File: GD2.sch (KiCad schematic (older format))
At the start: 19 parts, among them IC15 HCPL-316J, IC16 IXDD614PI, P16 CONN_01X03, P17 CONN_01X03

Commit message: uding HCPL-361J modified symbol
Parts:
- IC15: symbol HCPL-316J-RESCUE-gatedrive -> HCPL-316J
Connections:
- wire segments 41 -> 50
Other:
- moved on the sheet: IC16
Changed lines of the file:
@@
 EESchema Schematic File Version 2
-LIBS:gatedrive-rescue
 LIBS:power
 LIBS:device
@@
 LIBS:contrib
 LIBS:valves
-LIBS:GateDrive
+LIBS:74xgxx
+LIBS:ac-dc
+LIBS:actel
+LIBS:Altera
+LIBS:analog_devices
+LIBS:brooktre
+LIBS:cmos_ieee
+LIBS:dc-dc
+LIBS:diode
+LIBS:elec-unifil
+LIBS:ESD_Protection
+LIBS:ftdi
+LIBS:gennum
+LIBS:graphic
+LIBS:hc11
+LIBS:ir
+LIBS:Lattice
+LIBS:logo
+LIBS:maxim
+LIBS:microchip_dspic33dsc
+LIBS:microchip_pic10mcu
+LIBS:microchip_pic12mcu
+LIBS:microchip_pic16mcu
+LIBS:microchip_pic18mcu
+LIBS:microchip_pic32mcu
+LIBS:motor_drivers
+LIBS:msp430
+LIBS:nordicsemi
+LIBS:nxp_armmcu
+LIBS:onsemi
+LIBS:Oscillators
+LIBS:powerint
+LIBS:Power_Management
+LIBS:pspice
+LIBS:references
+LIBS:relays
+LIBS:rfcom
+LIBS:sensors
+LIBS:silabs
+LIBS:stm8
+LIBS:stm32
+LIBS:supertex
+LIBS:switches
+LIBS:transf
+LIBS:ttl_ieee
+LIBS:video
+LIBS:Worldsemi
+LIBS:Xicor
+LIBS:Zilog
 LIBS:gatedrive-cache
 EELAYER 25 0
@@
 L IXDD614PI-RESCUE-gatedrive IC16
 U 1 1 56EF8E42
-P 7900 5100
-F 0 "IC16" H 7900 4900 60  0000 C CNN
-F 1 "IXDD614PI" H 7950 5450 60  0000 C CNN
-F 2 "gatedrive:DIP-8_W7.62mm_LongPads" H 7900 5200 60  0001 C CNN
-F 3 "" H 7900 5200 60  0000 C CNN
-F 4 "CHINA[already bought]" H 7900 5100 60  0001 C CNN "Supplier"
-	1    7900 5100
-	1    0    0    -1
-$EndComp
-$Comp
-L HCPL-316J-RESCUE-gatedrive IC15
+P 7950 5100
+AR Path="/56EF8E42" Ref="IC16"  Part="1"
+AR Path="/56EF055C/56EF8E42" Ref="IC16"  Part="1"
+F 0 "IC16" H 7950 4900 60  0000 C CNN
+F 1 "IXDD614PI" H 8000 5450 60  0000 C CNN
+F 2 "gatedrive:DIP-8_W7.62mm_LongPads" H 7950 5200 60  0001 C CNN
+F 3 "" H 7950 5200 60  0000 C CNN
+F 4 "CHINA[already bought]" H 7950 5100 60  0001 C CNN "Supplier"
+	1    7950 5100
+	1    0    0    -1
+$EndComp
+$Comp
+L HCPL-316J IC15
 U 1 1 56EF8E43
-P 5550 4750
-F 0 "IC15" H 5550 4150 60  0000 C CNN
-F 1 "HCPL-316J" H 5300 5200 60  0000 C CNN
-F 2 "Housings_SOIC:SOIC-16_7.5x10.3mm_Pitch1.27mm" H 5550 4750 60  0001 C CNN
-F 3 "" H 5550 4750 60  0000 C CNN
-F 4 "CHINA [ already bought]" H 5550 4750 60  0001 C CNN "Supplier"
-	1    5550 4750
+P 5700 4850
+F 0 "IC15" H 5700 4400 60  0000 C CNN
+F 1 "HCPL-316J" H 5700 5450 60  0000 C CNN
+F 2 "Housings_SOIC:SOIC-16_7.5x10.3mm_Pitch1.27mm" H 5700 4850 60  0001 C CNN
+F 3 "" H 5700 4850 60  0000 C CNN
+F 4 "CHINA [ already bought]" H 5700 4850 60  0001 C CNN "Supplier"
+	1    5700 4850
 	1    0    0    -1
 $EndComp
@@
 a cap to ensure soft turn-off, recommended by datasheet of hcpl.
 Wire Wire Line
-	6950 4950 7500 4950
-Wire Wire Line
-	6250 4950 6650 4950
-Wire Wire Line
-	6250 5050 6250 5150
-Wire Wire Line
-	6250 4750 6250 4850
+	6950 4950 7150 4950
+Wire Wire Line
+	7150 4950 7550 4950
+Wire Wire Line
+	5900 4950 6500 4950
+Wire Wire Line
+	6500 4950 6650 4950
+Wire Wire Line
+	5900 5050 6250 5100
+Wire Wire Line
+	6250 5100 5900 5150
+Wire Wire Line
+	5900 4750 6250 4800
+Wire Wire Line
+	6250 4800 5900 4850
 Connection ~ 6550 4100
 Wire Wire Line
-	6550 4650 6250 4650
+	6550 4650 5900 4650
 Wire Wire Line
 	6550 4100 6650 4100
 Wire Wire Line
-	6550 4050 6550 4650
+	6550 4050 6550 4100
+Wire Wire Line
+	6550 4100 6550 4650
 Connection ~ 8450 4950
 Wire Wire Line
@@
 Connection ~ 7150 4950
 Wire Wire Line
-	3625 4650 4850 4650
-Wire Wire Line
-	8350 4950 9050 4950
+	3625 4650 4000 4650
+Wire Wire Line
+	4000 4650 5000 4650
+Wire Wire Line
+	8300 4950 8450 4950
+Wire Wire Line
+	8450 4950 8900 4950
+Wire Wire Line
+	8900 4950 9050 4950
 Wire Wire Line
 	9350 4950 9450 4950
 Wire Wire Line
-	9750 4950 10200 4950
+	9750 4950 9950 4950
+Wire Wire Line
+	9950 4950 10200 4950
 Wire Wire Line
 	9750 5250 9950 5250
@@
 Connection ~ 9950 4950
 Wire Wire Line
-	8350 5050 8450 5050
+	8300 5050 8450 5050
 Wire Wire Line
 	8450 5050 8450 4950
@@
 	4400 4350 4400 4550
 Wire Wire Line
-	4400 4550 4850 4550
+	4400 4550 5000 4550
 Wire Wire Line
 	4000 4350 4000 4650
@@
 	4000 5300 4000 4750
 Wire Wire Line
-	4000 4750 4850 4750
-Wire Wire Line
-	4850 5150 4750 5150
+	4000 4750 5000 4750
+Wire Wire Line
+	5000 5150 4750 5150
 Wire Wire Line
 	4750 5150 4750 5300
 Wire Wire Line
-	4850 4850 4400 4850
+	5000 4850 4400 4850
 Wire Wire Line
 	4400 4850 4400 5300
 Wire Wire Line
-	6250 4450 6300 4450
+	5900 4450 6300 4450
 Wire Wire Line
 	6300 4450 6300 4350
@@
 	6500 5000 6500 4950
 Wire Wire Line
-	7500 5050 7175 5050
+	7550 5050 7175 5050
 Wire Wire Line
 	7175 5050 7175 5075
 Text HLabel 900  3800 3    60   Input ~ 0
 T2
-Text HLabel 4850 4450 0    60   Input ~ 0
+Text HLabel 5000 4450 0    60   Input ~ 0
 T2
 Text GLabel 900  2650 3    60   Input ~ 0
@@
 Text GLabel 6600 2000 1    60   Input ~ 0
 ~FAULT
-Text GLabel 4850 4950 0    60   Input ~ 0
+Text GLabel 5000 4950 0    60   Input ~ 0
 ~FAULT
 Text GLabel 3625 4350 1    60   Input ~ 0
@@
 Text GLabel 7800 4400 2    60   Input ~ 0
 -5V2
-Text GLabel 8350 4850 2    60   Input ~ 0
+Text GLabel 8300 4850 2    60   Input ~ 0
 15V2
-Text GLabel 8350 5150 2    60   Input ~ 0
+Text GLabel 8300 5150 2    60   Input ~ 0
 -5V2
-Text GLabel 7500 5150 0    60   Input ~ 0
+Text GLabel 7550 5150 0    60   Input ~ 0
 -5V2
-Text GLabel 7500 4850 0    60   Input ~ 0
+Text GLabel 7550 4850 0    60   Input ~ 0
 15V2
 Text GLabel 7175 5075 3    60   Input ~ 0

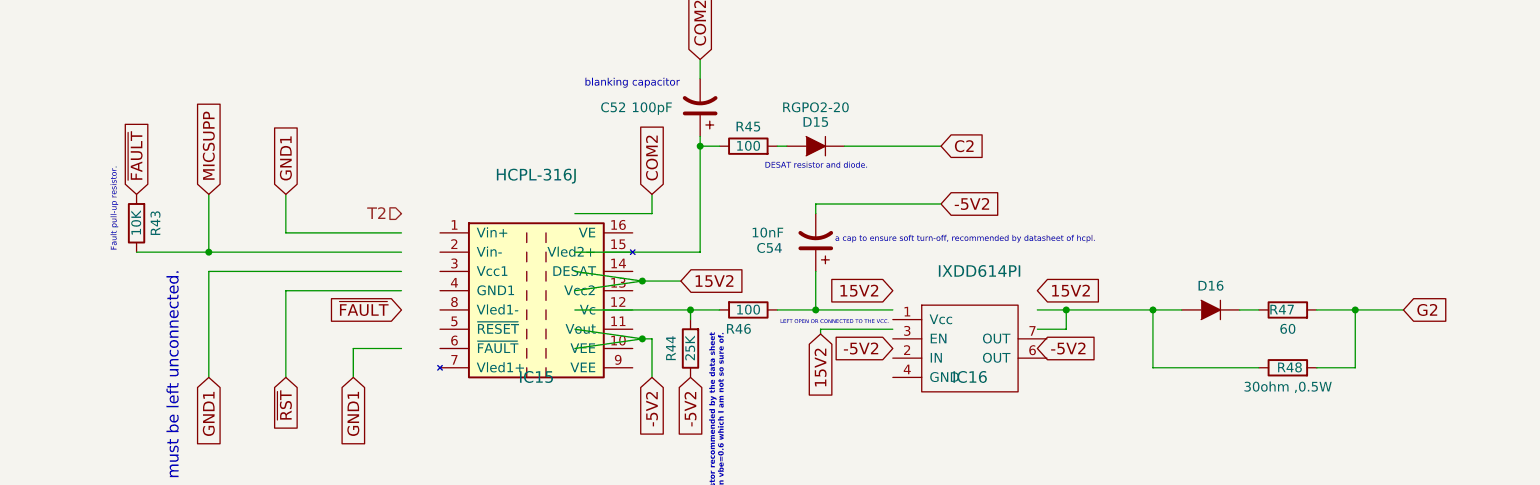
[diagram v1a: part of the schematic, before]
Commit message: cleaning the schematic
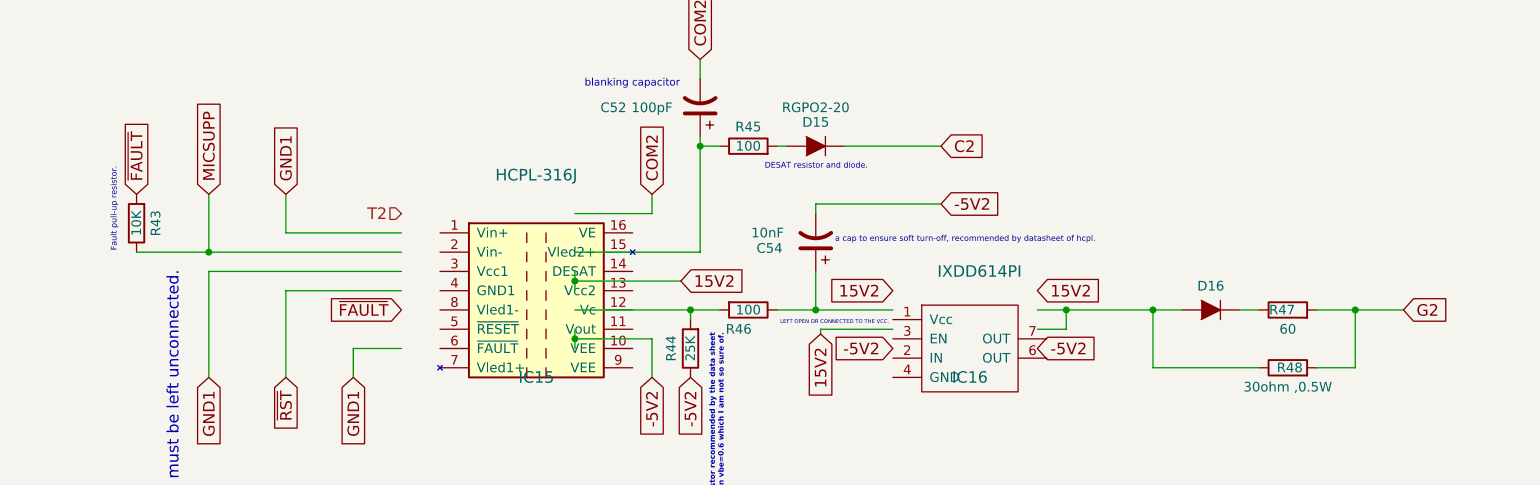
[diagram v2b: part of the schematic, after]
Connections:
- wire segments 50 -> 41
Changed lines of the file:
@@
 a cap to ensure soft turn-off, recommended by datasheet of hcpl.
 Wire Wire Line
-	6950 4950 7150 4950
+	6950 4950 7550 4950
 Wire Wire Line
-	7150 4950 7550 4950
+	5900 4950 6650 4950
 Wire Wire Line
-	5900 4950 6500 4950
+	5900 5050 5900 5150
 Wire Wire Line
-	6500 4950 6650 4950
-Wire Wire Line
-	5900 5050 6250 5100
-Wire Wire Line
-	6250 5100 5900 5150
-Wire Wire Line
-	5900 4750 6250 4800
-Wire Wire Line
-	6250 4800 5900 4850
+	5900 4750 5900 4850
 Connection ~ 6550 4100
 Wire Wire Line
@@
 	6550 4100 6650 4100
 Wire Wire Line
-	6550 4050 6550 4100
-Wire Wire Line
-	6550 4100 6550 4650
+	6550 4050 6550 4650
 Connection ~ 8450 4950
 Wire Wire Line
@@
 Connection ~ 7150 4950
 Wire Wire Line
-	3625 4650 4000 4650
+	3625 4650 5000 4650
 Wire Wire Line
-	4000 4650 5000 4650
-Wire Wire Line
-	8300 4950 8450 4950
-Wire Wire Line
-	8450 4950 8900 4950
-Wire Wire Line
-	8900 4950 9050 4950
+	8300 4950 9050 4950
 Wire Wire Line
 	9350 4950 9450 4950
 Wire Wire Line
-	9750 4950 9950 4950
-Wire Wire Line
-	9950 4950 10200 4950
+	9750 4950 10200 4950
 Wire Wire Line
 	9750 5250 9950 5250
@@
 	6300 5300 6300 5100
 Wire Wire Line
-	6300 5100 6250 5100
-Connection ~ 6250 5100
+	6300 5100 5900 5100
+Connection ~ 5900 5100
 Wire Wire Line
-	6250 4800 6450 4800
-Connection ~ 6250 4800
+	5900 4800 6450 4800
+Connection ~ 5900 4800
 Wire Wire Line
 	8900 5250 9450 5250

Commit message: completion of the layout, initial layout of the protection circuit, reducing number of circuit to 7
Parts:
- C50, C51, C52, C53, C54, C55, C56: footprint Capacitors_ThroughHole:C_Disc_D3_P2.5 -> gatedrive:C_Disc
- D15: footprint Diodes_ThroughHole:Diode_DO-201AD_Horizontal_RM15 -> Diodes_ThroughHole:Diode_DO-41_SOD81_Horizontal_RM10
- R43: footprint Resistors_ThroughHole:Resistor_Vertical_RM5mm -> Resistors_ThroughHole:Resistor_Horizontal_RM10mm
- R47, R48: footprint Resistors_ThroughHole:Resistor_Horizontal_RM20mm -> gatedrive:Resistor_multi
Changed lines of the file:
@@
 EESchema Schematic File Version 2
+LIBS:Symbols_DCDC-ACDC-Converter_RevC_20Jul2012
+LIBS:Symbols_EN60617_13Mar2013
+LIBS:Symbols_EN60617-10_HF-Radio_DRAFT_12Sep2013
+LIBS:Symbols_ICs-Diskrete_RevD10
+LIBS:Symbols_ICs-Opto_RevB_16Sep2013
+LIBS:Symbols_Microcontroller_Philips-NXP_RevA_06Oct2013
+LIBS:SymbolsSimilarEN60617+oldDIN617-RevE8
+LIBS:Symbols_Socket-DIN41612_RevA
+LIBS:Symbols_Transformer-Diskrete_RevA
 LIBS:power
 LIBS:device
@@
 $Descr A4 11693 8268
 encoding utf-8
-Sheet 9 10
+Sheet 9 9
 Title "IGBT GATE DRIVE SCHEMATIC."
 Date "2016-03-02"
@@
 F 0 "D15" H 7150 3976 50  0000 C CNN
 F 1 "RGPO2-20" H 7150 3900 50  0000 C CNN
-F 2 "Diodes_ThroughHole:Diode_DO-201AD_Horizontal_RM15" H 7150 4100 50  0001 C CNN
+F 2 "Diodes_ThroughHole:Diode_DO-41_SOD81_Horizontal_RM10" H 7150 4100 50  0001 C CNN
 F 3 "" H 7150 4100 50  0000 C CNN
 F 4 "El-Amir" H 7150 4100 60  0001 C CNN "Supplier"
@@
 F 0 "R43" V 3525 4500 50  0000 C CNN
 F 1 "10K" V 3625 4500 50  0000 C CNN
-F 2 "Resistors_ThroughHole:Resistor_Vertical_RM5mm" V 3555 4500 50  0001 C CNN
+F 2 "Resistors_ThroughHole:Resistor_Horizontal_RM10mm" V 3555 4500 50  0001 C CNN
 F 3 "" H 3625 4500 50  0000 C CNN
 F 4 "EL AMIR" H 3625 4500 60  0001 C CNN "Supplier"
@@
 F 0 "C50" H 4150 2150 50  0000 C CNN
 F 1 "0.1uF" H 4250 2050 50  0000 C CNN
-F 2 "Capacitors_ThroughHole:C_Disc_D3_P2.5" H 4488 2000 50  0001 C CNN
+F 2 "gatedrive:C_Disc" H 4488 2000 50  0001 C CNN
 F 3 "" H 4450 2150 50  0000 C CNN
 F 4 "EL AMIR" H 4450 2150 60  0001 C CNN "Supplier"
@@
 F 0 "C52" H 7000 3900 50  0000 C CNN
 F 1 "100pF" H 6800 3900 50  0000 C CNN
-F 2 "Capacitors_ThroughHole:C_Disc_D3_P2.5" H 6588 3750 50  0001 C CNN
+F 2 "gatedrive:C_Disc" H 6588 3750 50  0001 C CNN
 F 3 "" H 6550 3900 50  0000 C CNN
 	1    6550 3900
@@
 F 0 "C56" H 8450 2150 50  0000 C CNN
 F 1 "0.1uF" H 8450 2050 50  0000 C CNN
-F 2 "Capacitors_ThroughHole:C_Disc_D3_P2.5" H 8888 2000 50  0001 C CNN
+F 2 "gatedrive:C_Disc" H 8888 2000 50  0001 C CNN
 F 3 "" H 8850 2150 50  0000 C CNN
 	1    8850 2150
@@
 F 0 "C55" H 7400 2150 50  0000 C CNN
 F 1 "0.1uF" H 7400 2050 50  0000 C CNN
-F 2 "Capacitors_ThroughHole:C_Disc_D3_P2.5" H 7788 2000 50  0001 C CNN
+F 2 "gatedrive:C_Disc" H 7788 2000 50  0001 C CNN
 F 3 "" H 7750 2150 50  0000 C CNN
 	1    7750 2150
@@
 F 0 "C51" H 5150 2150 50  0000 C CNN
 F 1 "0.1uF" H 5150 2050 50  0000 C CNN
-F 2 "Capacitors_ThroughHole:C_Disc_D3_P2.5" H 5538 2000 50  0001 C CNN
+F 2 "gatedrive:C_Disc" H 5538 2000 50  0001 C CNN
 F 3 "" H 5500 2150 50  0000 C CNN
 	1    5500 2150
@@
 F 0 "C53" H 6300 2150 50  0000 R CNN
 F 1 "330pF" H 6400 2050 50  0000 R CNN
-F 2 "Capacitors_ThroughHole:C_Disc_D3_P2.5" H 6638 2000 50  0001 C CNN
+F 2 "gatedrive:C_Disc" H 6638 2000 50  0001 C CNN
 F 3 "" H 6600 2150 50  0000 C CNN
 	1    6600 2150
@@
 LEFT OPEN OR CONNECTED TO THE VCC.
 $Comp
-L PWR_FLAG #FLG050
+L PWR_FLAG #FLG036
 U 1 1 56EF8E50
 P 1300 3800
-F 0 "#FLG050" H 1300 3895 50  0001 C CNN
+F 0 "#FLG036" H 1300 3895 50  0001 C CNN
 F 1 "PWR_FLAG" H 1300 4024 50  0000 C CNN
 F 2 "" H 1300 3800 50  0000 C CNN
@@
 $EndComp
 $Comp
-L PWR_FLAG #FLG051
+L PWR_FLAG #FLG037
 U 1 1 56EF8E51
 P 1750 3800
-F 0 "#FLG051" H 1750 3895 50  0001 C CNN
+F 0 "#FLG037" H 1750 3895 50  0001 C CNN
 F 1 "PWR_FLAG" H 1750 4024 50  0000 C CNN
 F 2 "" H 1750 3800 50  0000 C CNN
@@
 $EndComp
 $Comp
-L PWR_FLAG #FLG052
+L PWR_FLAG #FLG038
 U 1 1 56EF8E52
 P 1750 2650
-F 0 "#FLG052" H 1750 2745 50  0001 C CNN
+F 0 "#FLG038" H 1750 2745 50  0001 C CNN
 F 1 "PWR_FLAG" H 1750 2874 50  0000 C CNN
 F 2 "" H 1750 2650 50  0000 C CNN
@@
 $EndComp
 $Comp
-L PWR_FLAG #FLG053
+L PWR_FLAG #FLG039
 U 1 1 56EF8E53
 P 900 2650
-F 0 "#FLG053" H 900 2745 50  0001 C CNN
+F 0 "#FLG039" H 900 2745 50  0001 C CNN
 F 1 "PWR_FLAG" H 900 2874 50  0000 C CNN
 F 2 "" H 900 2650 50  0000 C CNN
@@
 $EndComp
 $Comp
-L PWR_FLAG #FLG054
+L PWR_FLAG #FLG040
 U 1 1 56EF8E54
 P 1300 2650
-F 0 "#FLG054" H 1300 2745 50  0001 C CNN
+F 0 "#FLG040" H 1300 2745 50  0001 C CNN
 F 1 "PWR_FLAG" H 1300 2874 50  0000 C CNN
 F 2 "" H 1300 2650 50  0000 C CNN
@@
 $EndComp
 $Comp
-L PWR_FLAG #FLG055
+L PWR_FLAG #FLG041
 U 1 1 56EF8E55
 P 900 3800
-F 0 "#FLG055" H 900 3895 50  0001 C CNN
+F 0 "#FLG041" H 900 3895 50  0001 C CNN
 F 1 "PWR_FLAG" H 900 4024 50  0000 C CNN
 F 2 "" H 900 3800 50  0000 C CNN
@@
 F 0 "C54" H 7390 4630 50  0000 C CNN
 F 1 "10nF" H 7400 4550 50  0000 C CNN
-F 2 "Capacitors_ThroughHole:C_Disc_D3_P2.5" H 7188 4450 50  0001 C CNN
+F 2 "gatedrive:C_Disc" H 7188 4450 50  0001 C CNN
 F 3 "" H 7150 4600 50  0000 C CNN
 	1    7150 4600
@@
 F 0 "R47" V 9600 4980 50  0000 C CNN
 F 1 "60" V 9500 4950 50  0000 C CNN
-F 2 "Resistors_ThroughHole:Resistor_Horizontal_RM20mm" V 9530 4950 50  0001 C CNN
+F 2 "gatedrive:Resistor_multi" V 9530 4950 50  0001 C CNN
 F 3 "" H 9600 4950 50  0000 C CNN
 F 4 "Al amir" H 9600 4950 60  0001 C CNN "Supplier"
@@
 F 0 "R48" V 9600 5240 50  0000 C CNN
 F 1 "30ohm ,0.5W" V 9500 5250 50  0000 C CNN
-F 2 "Resistors_ThroughHole:Resistor_Horizontal_RM20mm" V 9530 5250 50  0001 C CNN
+F 2 "gatedrive:Resistor_multi" V 9530 5250 50  0001 C CNN
 F 3 "" H 9600 5250 50  0000 C CNN
 F 4 "Supplier_name" H 9600 5250 60  0001 C CNN "Supplier"
@@
 	6950 4100 7000 4100
 $Comp
-L PWR_FLAG #FLG056
+L PWR_FLAG #FLG042
 U 1 1 56EF8E5C
 P 1475 3050
-F 0 "#FLG056" H 1475 3145 50  0001 C CNN
+F 0 "#FLG042" H 1475 3145 50  0001 C CNN
 F 1 "PWR_FLAG" V 1625 3050 50  0000 C CNN
 F 2 "" H 1475 3050 50  0000 C CNN

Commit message: yet another enhancements .
the protection section still is incomplete.
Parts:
- IC16: symbol IXDD614PI-RESCUE-gatedrive -> IXDD614PI
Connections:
- wire segments 41 -> 50
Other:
- moved on the sheet: IC15
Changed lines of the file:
@@
 $Descr A4 11693 8268
 encoding utf-8
-Sheet 9 9
+Sheet 7 9
 Title "IGBT GATE DRIVE SCHEMATIC."
 Date "2016-03-02"
@@
 $EndDescr
 $Comp
-L IXDD614PI-RESCUE-gatedrive IC16
+L IXDD614PI IC16
 U 1 1 56EF8E42
-P 7950 5100
+P 7950 4950
 AR Path="/56EF8E42" Ref="IC16"  Part="1"
 AR Path="/56EF055C/56EF8E42" Ref="IC16"  Part="1"
-F 0 "IC16" H 7950 4900 60  0000 C CNN
-F 1 "IXDD614PI" H 8000 5450 60  0000 C CNN
-F 2 "gatedrive:DIP-8_W7.62mm_LongPads" H 7950 5200 60  0001 C CNN
-F 3 "" H 7950 5200 60  0000 C CNN
-F 4 "CHINA[already bought]" H 7950 5100 60  0001 C CNN "Supplier"
-	1    7950 5100
+F 0 "IC16" H 7950 4750 60  0000 C CNN
+F 1 "IXDD614PI" H 8000 5300 60  0000 C CNN
+F 2 "gatedrive:DIP-8_W7.62mm_LongPads" H 7950 5050 60  0001 C CNN
+F 3 "" H 7950 5050 60  0000 C CNN
+F 4 "CHINA[already bought]" H 7950 4950 60  0001 C CNN "Supplier"
+	1    7950 4950
 	1    0    0    -1
 $EndComp
@@
 L HCPL-316J IC15
 U 1 1 56EF8E43
-P 5700 4850
-F 0 "IC15" H 5700 4400 60  0000 C CNN
-F 1 "HCPL-316J" H 5700 5450 60  0000 C CNN
-F 2 "Housings_SOIC:SOIC-16_7.5x10.3mm_Pitch1.27mm" H 5700 4850 60  0001 C CNN
-F 3 "" H 5700 4850 60  0000 C CNN
-F 4 "CHINA [ already bought]" H 5700 4850 60  0001 C CNN "Supplier"
-	1    5700 4850
+P 5400 4750
+AR Path="/56EF8E43" Ref="IC15"  Part="1"
+AR Path="/56EF055C/56EF8E43" Ref="IC15"  Part="1"
+F 0 "IC15" H 5400 4300 60  0000 C CNN
+F 1 "HCPL-316J" H 5400 5350 60  0000 C CNN
+F 2 "Housings_SOIC:SOIC-16_7.5x10.3mm_Pitch1.27mm" H 5400 4750 60  0001 C CNN
+F 3 "" H 5400 4750 60  0000 C CNN
+F 4 "CHINA [ already bought]" H 5400 4750 60  0001 C CNN "Supplier"
+	1    5400 4750
 	1    0    0    -1
 $EndComp
@@
 a cap to ensure soft turn-off, recommended by datasheet of hcpl.
 Wire Wire Line
-	6950 4950 7550 4950
-Wire Wire Line
-	5900 4950 6650 4950
-Wire Wire Line
-	5900 5050 5900 5150
-Wire Wire Line
-	5900 4750 5900 4850
+	6950 4950 7150 4950
+Wire Wire Line
+	7150 4950 7550 4950
+Wire Wire Line
+	5900 4950 6500 4950
+Wire Wire Line
+	6500 4950 6650 4950
+Wire Wire Line
+	5900 5050 5900 5100
+Wire Wire Line
+	5900 5100 5900 5150
+Wire Wire Line
+	5900 4750 5900 4800
+Wire Wire Line
+	5900 4800 5900 4850
 Connection ~ 6550 4100
 Wire Wire Line
@@
 	6550 4100 6650 4100
 Wire Wire Line
-	6550 4050 6550 4650
+	6550 4050 6550 4100
+Wire Wire Line
+	6550 4100 6550 4650
 Connection ~ 8450 4950
 Wire Wire Line
@@
 Connection ~ 7150 4950
 Wire Wire Line
-	3625 4650 5000 4650
-Wire Wire Line
-	8300 4950 9050 4950
+	3625 4650 4000 4650
+Wire Wire Line
+	4000 4650 4900 4650
+Wire Wire Line
+	8350 4950 8450 4950
+Wire Wire Line
+	8450 4950 8900 4950
+Wire Wire Line
+	8900 4950 9050 4950
 Wire Wire Line
 	9350 4950 9450 4950
 Wire Wire Line
-	9750 4950 10200 4950
+	9750 4950 9950 4950
+Wire Wire Line
+	9950 4950 10200 4950
 Wire Wire Line
 	9750 5250 9950 5250
@@
 Connection ~ 9950 4950
 Wire Wire Line
-	8300 5050 8450 5050
+	8350 5050 8450 5050
 Wire Wire Line
 	8450 5050 8450 4950
@@
 	4400 4350 4400 4550
 Wire Wire Line
-	4400 4550 5000 4550
+	4400 4550 4900 4550
 Wire Wire Line
 	4000 4350 4000 4650
@@
 	4000 5300 4000 4750
 Wire Wire Line
-	4000 4750 5000 4750
-Wire Wire Line
-	5000 5150 4750 5150
+	4000 4750 4900 4750
+Wire Wire Line
+	4900 5150 4750 5150
 Wire Wire Line
 	4750 5150 4750 5300
 Wire Wire Line
-	5000 4850 4400 4850
+	4900 4850 4400 4850
 Wire Wire Line
 	4400 4850 4400 5300
@@
 Text HLabel 900  3800 3    60   Input ~ 0
 T2
-Text HLabel 5000 4450 0    60   Input ~ 0
+Text HLabel 4900 4450 0    60   Input ~ 0
 T2
 Text GLabel 900  2650 3    60   Input ~ 0
@@
 Text GLabel 6600 2000 1    60   Input ~ 0
 ~FAULT
-Text GLabel 5000 4950 0    60   Input ~ 0
+Text GLabel 4900 4950 0    60   Input ~ 0
 ~FAULT
 Text GLabel 3625 4350 1    60   Input ~ 0
@@
 Text GLabel 7800 4400 2    60   Input ~ 0
 -5V2
-Text GLabel 8300 4850 2    60   Input ~ 0
+Text GLabel 8350 4850 2    60   Input ~ 0
 15V2
-Text GLabel 8300 5150 2    60   Input ~ 0
+Text GLabel 8350 5150 2    60   Input ~ 0
 -5V2
 Text GLabel 7550 5150 0    60   Input ~ 0
